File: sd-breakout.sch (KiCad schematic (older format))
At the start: 5 parts, among them J1 Header, J2 microSD Socket, U1 EClamp2410P

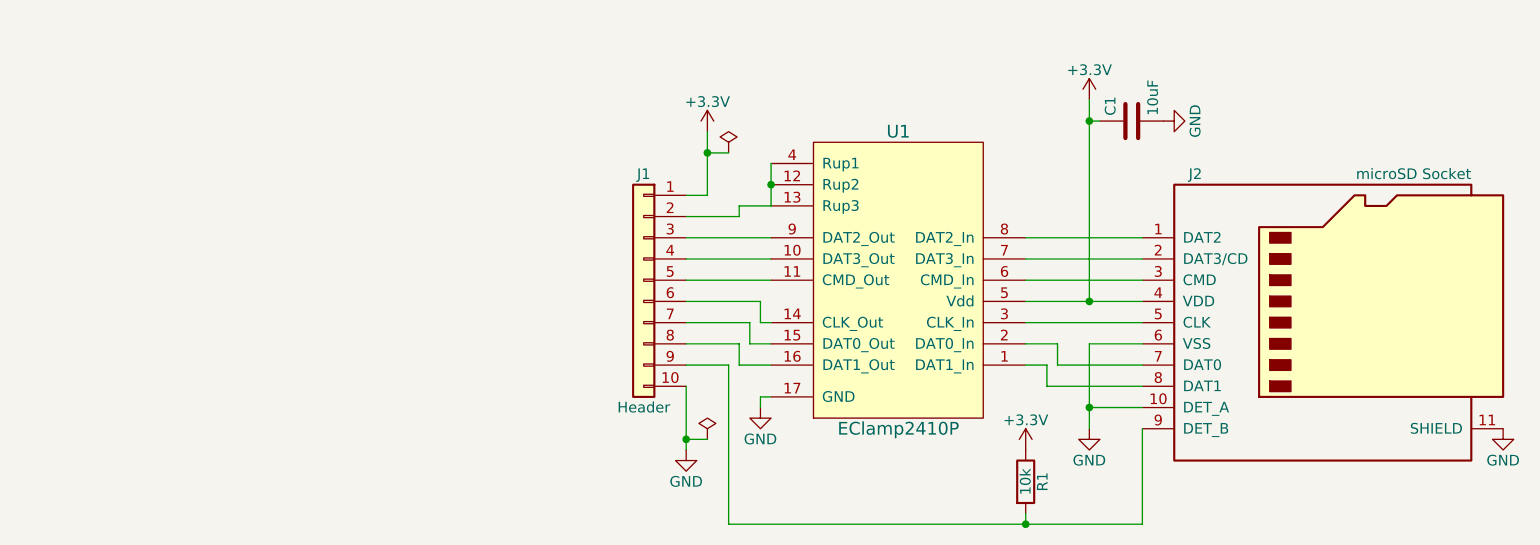
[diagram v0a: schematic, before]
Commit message: Finished layout and added logos
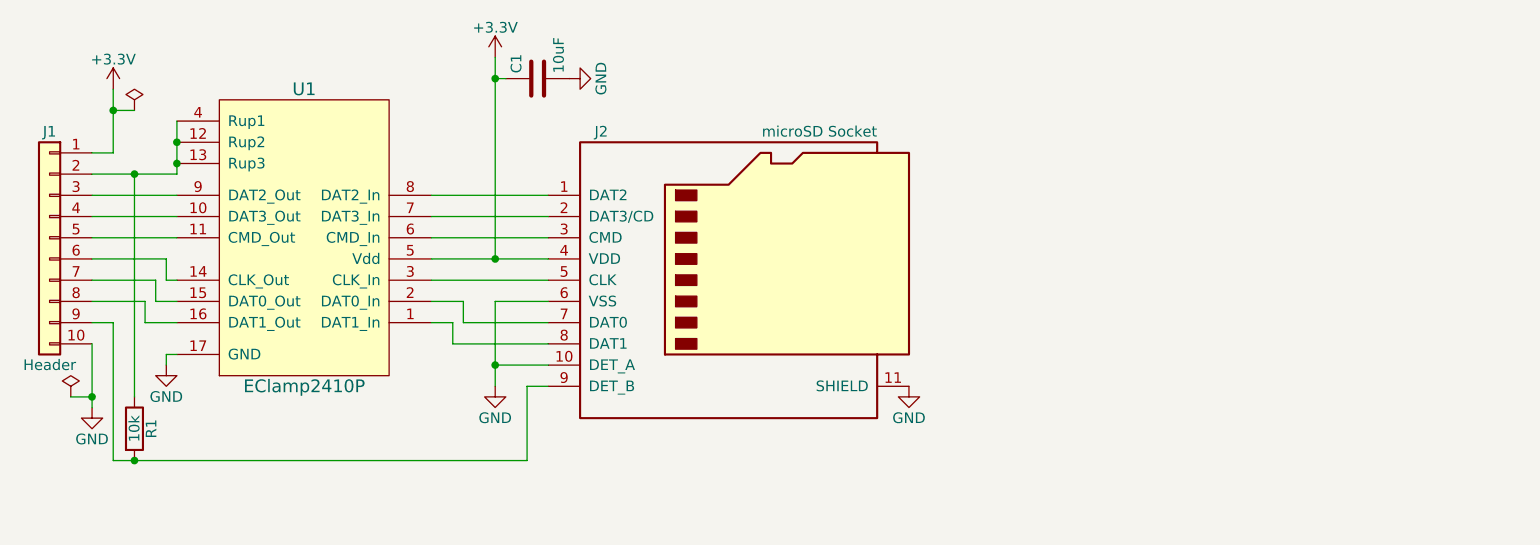
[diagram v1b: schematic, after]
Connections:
- net +3V3: no longer R1.1
- net at J1.2 (Pin_2), U1.12 (Rup2), U1.13 (Rup3)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: now also R1.1
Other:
- moved on the sheet: C1, J1, J2, R1, U1
